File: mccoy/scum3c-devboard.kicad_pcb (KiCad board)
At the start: 2 copper layers, 42.5 x 34.3 mm, 44 parts, among them J1 Conn_02x06_Odd_Even, J10 through_hole, J11 through_hole, J12 through_hole, J13 through_hole, J14 through_hole, J15 through_hole, J16 through_hole, J17 through_hole, J18 through_hole, J19 through_hole, J2 Conn_02x10_Odd_Even, J20 through_hole, J21 through_hole, J3 Conn_02x06_Odd_Even, J4 Conn_01x01_Male, J5 through_hole, J6 through_hole, J7 through_hole, J8 through_hole, J9 through_hole, U1 scum3, U9AB1 ICM-20948

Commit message: added some labels for clarity
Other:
- board text added: "P0.15"

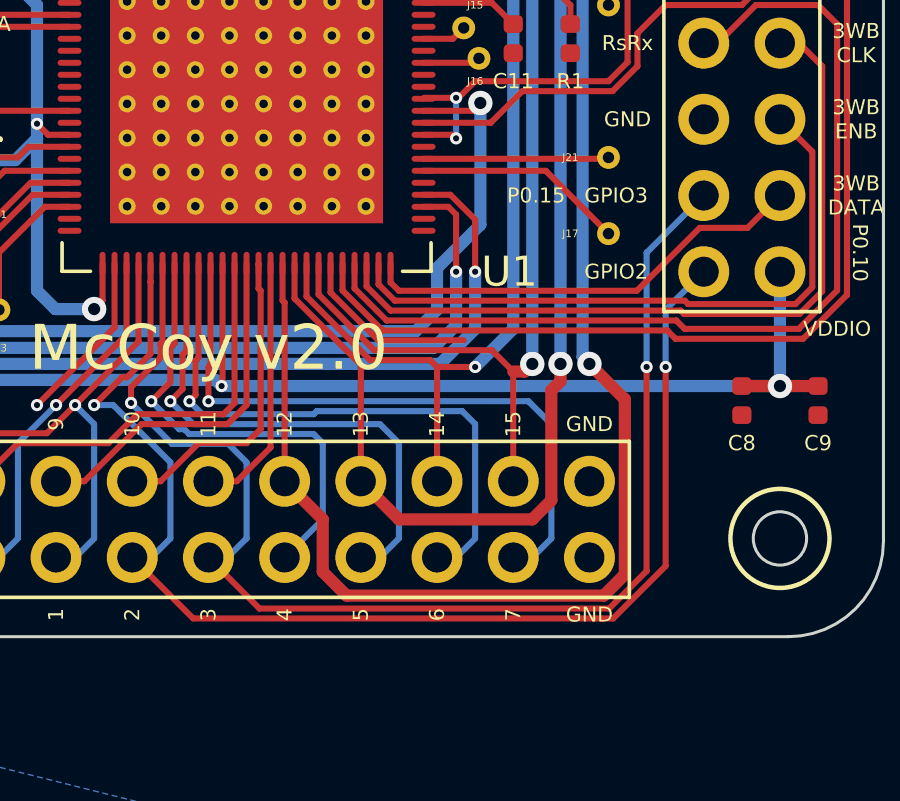
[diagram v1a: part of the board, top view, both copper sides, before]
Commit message: swapped around GPIO 2 and 3 for nrf
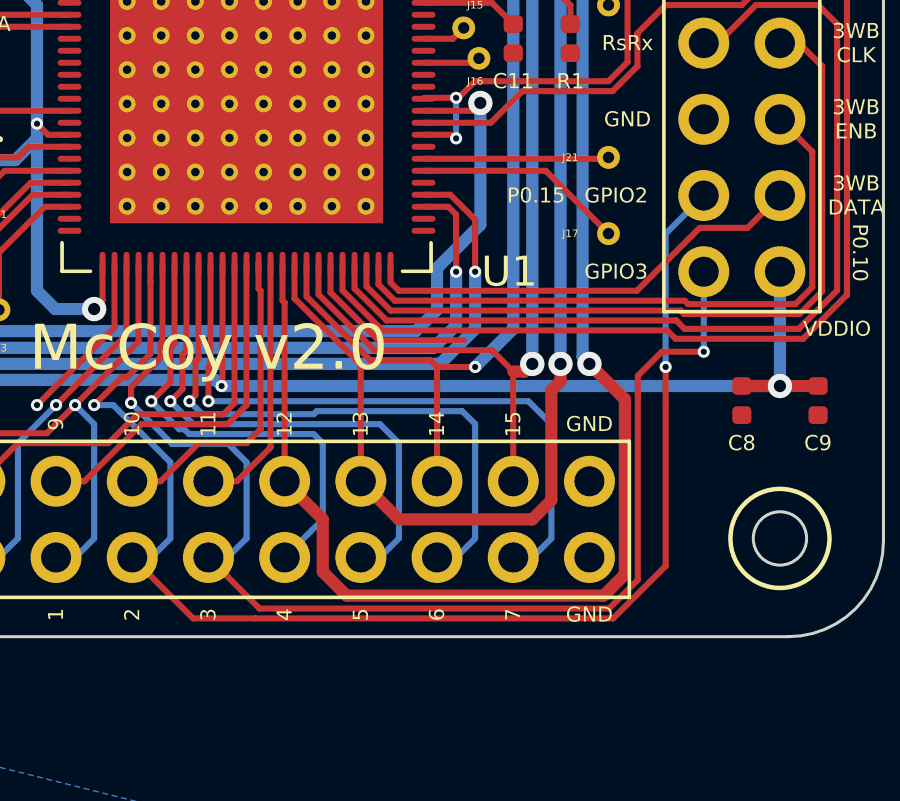
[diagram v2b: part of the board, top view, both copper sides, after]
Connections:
- J3 pad 11: /GPIO2 -> /GPIO3
- J3 pad 9: /GPIO3 -> /GPIO2
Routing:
- net /GPIO2: track 42.7 -> 45.2 mm
- net /GPIO3: track 42.9 -> 41.3 mm
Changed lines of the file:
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@@
     (thickness 1.6)
     (drawings 772)
-    (tracks 454)
+    (tracks 459)
     (zones 0)
     (modules 44)
@@
   (page A4)
   (layers
-    (0 F.Cu mixed hide)
-    (31 B.Cu mixed hide)
-    (32 B.Adhes user hide)
-    (33 F.Adhes user hide)
+    (0 F.Cu mixed)
+    (31 B.Cu mixed)
+    (32 B.Adhes user)
+    (33 F.Adhes user)
     (34 B.Paste user hide)
-    (35 F.Paste user hide)
+    (35 F.Paste user)
     (36 B.SilkS user)
     (37 F.SilkS user)
     (38 B.Mask user)
     (39 F.Mask user hide)
-    (40 Dwgs.User user hide)
-    (41 Cmts.User user hide)
-    (42 Eco1.User user hide)
-    (43 Eco2.User user hide)
+    (40 Dwgs.User user)
+    (41 Cmts.User user)
+    (42 Eco1.User user)
+    (43 Eco2.User user)
     (44 Edge.Cuts user)
-    (45 Margin user hide)
-    (46 B.CrtYd user hide)
+    (45 Margin user)
+    (46 B.CrtYd user)
     (47 F.CrtYd user)
-    (48 B.Fab user hide)
-    (49 F.Fab user hide)
+    (48 B.Fab user)
+    (49 F.Fab user)
   )
   (setup
@@
       (net 4 +VDDIO))
     (pad 11 thru_hole oval (at 0 12.7) (size 1.7 1.7) (drill 1) (layers *.Cu *.Mask)
-      (net 13 /GPIO2))
+      (net 9 /GPIO3))
     (pad 10 thru_hole oval (at 2.54 10.16) (size 1.7 1.7) (drill 1) (layers *.Cu *.Mask)
       (net 15 /3WB_DATA))
     (pad 9 thru_hole oval (at 0 10.16) (size 1.7 1.7) (drill 1) (layers *.Cu *.Mask)
-      (net 9 /GPIO3))
+      (net 13 /GPIO2))
     (pad 8 thru_hole oval (at 2.54 7.62) (size 1.7 1.7) (drill 1) (layers *.Cu *.Mask)
       (net 16 /3WB_ENB))
@@
     (effects (font (size 0.5 0.5) (thickness 0.1)) (justify mirror))
   )
-  (gr_text GPIO2 (at 138.684 96.52) (layer F.SilkS)
-    (effects (font (size 0.5 0.5) (thickness 0.1)))
-  )
-  (gr_text GPIO2 (at 138.684 96.52) (layer B.SilkS)
-    (effects (font (size 0.5 0.5) (thickness 0.1)) (justify mirror))
-  )
-  (gr_text GPIO3 (at 138.684 93.98) (layer F.SilkS)
-    (effects (font (size 0.5 0.5) (thickness 0.1)))
-  )
-  (gr_text GPIO3 (at 138.684 93.98) (layer B.SilkS)
+  (gr_text GPIO2 (at 138.684 93.98) (layer F.SilkS)
+    (effects (font (size 0.5 0.5) (thickness 0.1)))
+  )
+  (gr_text GPIO2 (at 138.684 93.98) (layer B.SilkS)
+    (effects (font (size 0.5 0.5) (thickness 0.1)) (justify mirror))
+  )
+  (gr_text GPIO3 (at 138.684 96.52) (layer F.SilkS)
+    (effects (font (size 0.5 0.5) (thickness 0.1)))
+  )
+  (gr_text GPIO3 (at 138.684 96.52) (layer B.SilkS)
     (effects (font (size 0.5 0.5) (thickness 0.1)) (justify mirror))
   )
@@
   (segment (start 125.73 106.045) (end 125.095 106.045) (width 0.2032) (layer B.Cu) (net 9) (status 30))
   (segment (start 126.365 105.41) (end 125.73 106.045) (width 0.2032) (layer B.Cu) (net 9) (status 20))
-  (via (at 139.7 99.695) (size 0.4064) (drill 0.2032) (layers F.Cu B.Cu) (net 9))
-  (segment (start 138.450559 107.74681) (end 139.7 106.497369) (width 0.2032) (layer F.Cu) (net 9))
-  (segment (start 139.7 106.497369) (end 139.7 99.695) (width 0.2032) (layer F.Cu) (net 9))
+  (segment (start 138.450559 107.74681) (end 139.407011 106.790358) (width 0.2032) (layer F.Cu) (net 9))
   (segment (start 125.095 106.045) (end 126.79681 107.74681) (width 0.2032) (layer F.Cu) (net 9))
   (segment (start 126.79681 107.74681) (end 138.450559 107.74681) (width 0.2032) (layer F.Cu) (net 9))
-  (segment (start 139.7 95.885) (end 141.605 93.98) (width 0.2032) (layer B.Cu) (net 9))
-  (segment (start 139.7 99.695) (end 139.7 95.885) (width 0.2032) (layer B.Cu) (net 9))
+  (via (at 141.605 99.18701) (size 0.4064) (drill 0.2032) (layers F.Cu B.Cu) (net 9))
+  (segment (start 141.605 99.18701) (end 141.605 96.52) (width 0.2032) (layer B.Cu) (net 9))
+  (segment (start 141.605 99.18701) (end 140.20799 99.18701) (width 0.2032) (layer F.Cu) (net 9))
+  (segment (start 140.20799 99.18701) (end 139.407011 99.987989) (width 0.2032) (layer F.Cu) (net 9))
+  (segment (start 139.407011 99.987989) (end 139.407011 100.622989) (width 0.2032) (layer F.Cu) (net 9))
+  (segment (start 139.407011 106.790358) (end 139.407011 100.622989) (width 0.2032) (layer F.Cu) (net 9))
+  (segment (start 139.407011 100.622989) (end 139.407011 100.59474) (width 0.2032) (layer F.Cu) (net 9))
   (via (at 120.65 100.965) (size 0.4064) (drill 0.2032) (layers F.Cu B.Cu) (net 10))
   (segment (start 122.765 96.255) (end 122.765 98.85) (width 0.2032) (layer F.Cu) (net 10) (status 10))
@@
   (segment (start 121.92 100.965) (end 121.285 100.965) (width 0.2032) (layer B.Cu) (net 13))
   (segment (start 123.19 106.045) (end 123.825 105.41) (width 0.2032) (layer B.Cu) (net 13) (status 10))
+  (segment (start 124.58702 108.07702) (end 126.660033 108.07702) (width 0.2032) (layer F.Cu) (net 13))
+  (segment (start 122.555 106.045) (end 124.58702 108.07702) (width 0.2032) (layer F.Cu) (net 13))
+  (segment (start 138.587336 108.07702) (end 140.335 106.329356) (width 0.2032) (layer F.Cu) (net 13))
+  (segment (start 126.660033 108.07702) (end 138.587336 108.07702) (width 0.2032) (layer F.Cu) (net 13))
+  (segment (start 140.335 106.329356) (end 140.335 100.965) (width 0.2032) (layer F.Cu) (net 13))
   (via (at 140.335 99.695) (size 0.4064) (drill 0.2032) (layers F.Cu B.Cu) (net 13))
-  (segment (start 138.587336 108.07702) (end 140.335 106.329356) (width 0.2032) (layer F.Cu) (net 13))
-  (segment (start 122.555 106.045) (end 124.58702 108.07702) (width 0.2032) (layer F.Cu) (net 13))
-  (segment (start 140.335 106.329356) (end 140.335 99.695) (width 0.2032) (layer F.Cu) (net 13))
-  (segment (start 124.58702 108.07702) (end 138.587336 108.07702) (width 0.2032) (layer F.Cu) (net 13))
-  (segment (start 140.335 97.79) (end 141.605 96.52) (width 0.2032) (layer B.Cu) (net 13))
-  (segment (start 140.335 99.695) (end 140.335 97.79) (width 0.2032) (layer B.Cu) (net 13))
+  (segment (start 140.335 100.965) (end 140.335 99.695) (width 0.2032) (layer F.Cu) (net 13))
+  (segment (start 140.335 95.25) (end 141.605 93.98) (width 0.2032) (layer B.Cu) (net 13))
+  (segment (start 140.335 99.695) (end 140.335 95.25) (width 0.2032) (layer B.Cu) (net 13))
   (via (at 120.015 100.965) (size 0.4064) (drill 0.2032) (layers F.Cu B.Cu) (net 14))
   (segment (start 122.365 96.255) (end 122.365 98.615) (width 0.2032) (layer F.Cu) (net 14) (status 10))

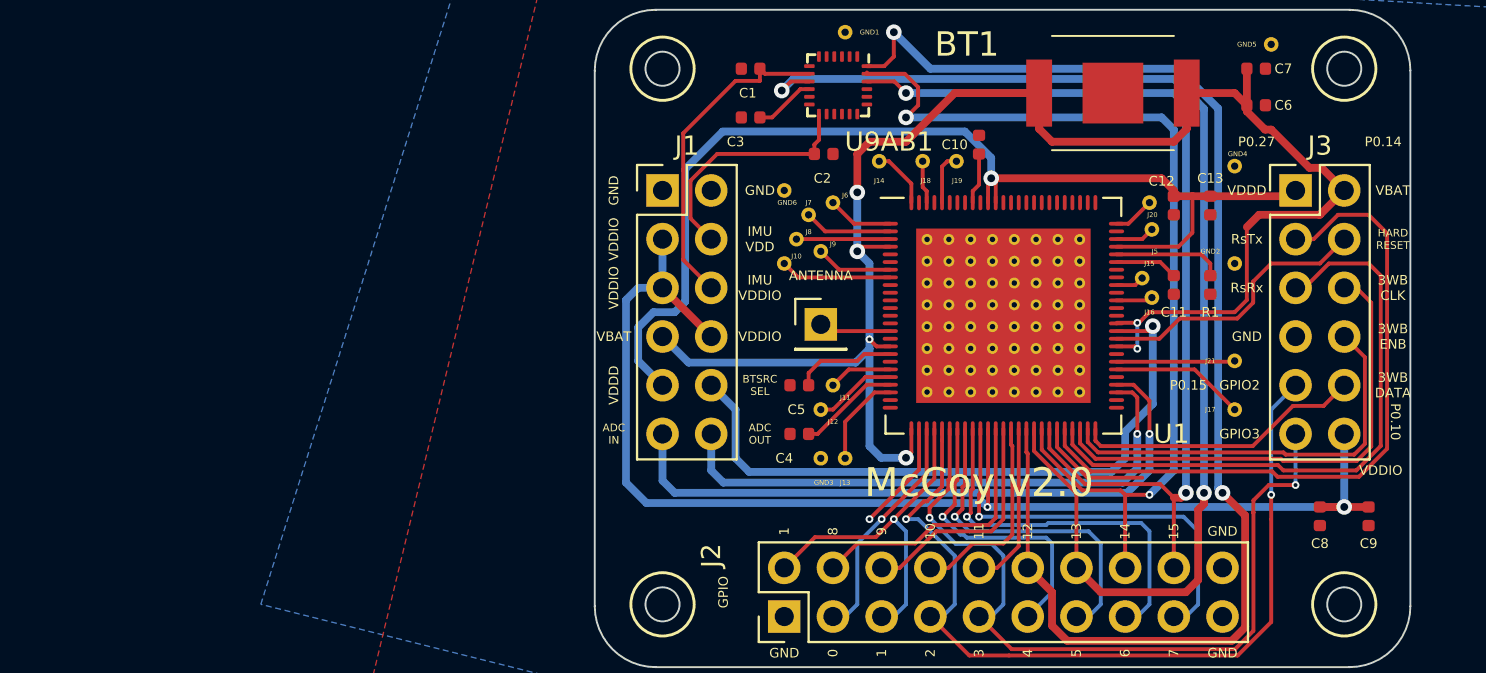
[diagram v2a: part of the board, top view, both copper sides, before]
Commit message: added a regulator to layout
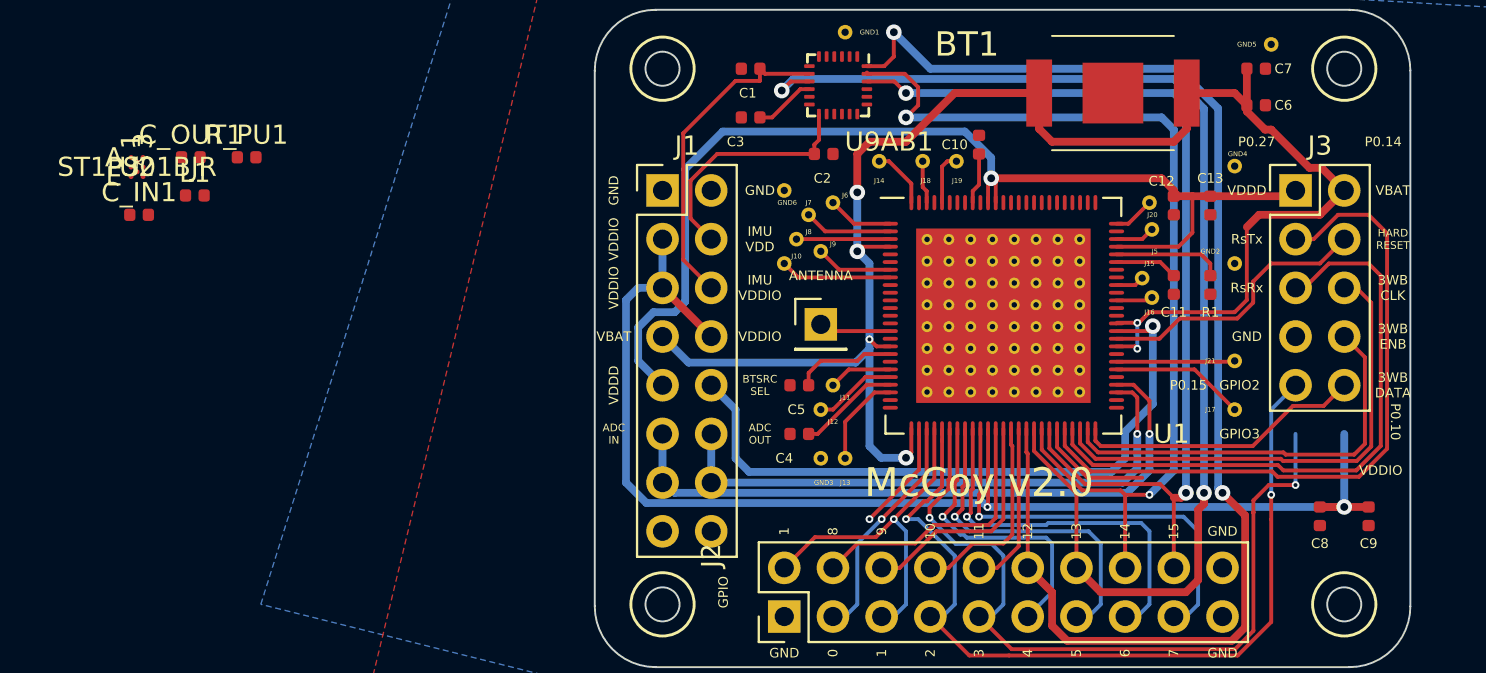
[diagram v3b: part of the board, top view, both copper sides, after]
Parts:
- added C_IN1: 10 uF, Capacitor_SMD:C_0402_1005Metric, F.Cu at (81.3, 85.1)
- added C_OUT1: 10 uF, Capacitor_SMD:C_0402_1005Metric, F.Cu at (84.0, 82.1)
- added L1: 2.2 uH, Inductor_SMD:L_0402_1005Metric, F.Cu at (84.2, 84.1)
- added R_PU1: 1M, Resistor_SMD:R_0402_1005Metric, F.Cu at (86.9, 82.1)
- added U2: ST1PS01BJR, regulator:ST1PS01BJR, F.Cu at (81.2, 82.6)
- J1: value Conn_02x06_Odd_Even -> Conn_02x08_Odd_Even; footprint Connector_PinHeader_2.54mm:PinHeader_2x06_P2.54mm_Vertical -> Connector_PinHeader_2.54mm:PinHeader_2x08_P2.54mm_Vertical
- J3: value Conn_02x06_Odd_Even -> Conn_02x05_Odd_Even; footprint Connector_PinHeader_2.54mm:PinHeader_2x06_P2.54mm_Vertical -> Connector_PinHeader_2.54mm:PinHeader_2x05_P2.54mm_Vertical
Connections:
- U1 pad 10: (no net) -> +VDD25
- U1 pad 12: (no net) -> Net-(U1-Pad12)
- U1 pad 13: (no net) -> Net-(U1-Pad13)
- U1 pad 19: (no net) -> Net-(U1-Pad19)
- U1 pad 24: (no net) -> Net-(U1-Pad24)
- U1 pad 25: (no net) -> Net-(U1-Pad25)
- U1 pad 51: (no net) -> Net-(U1-Pad51)
- U1 pad 52: (no net) -> Net-(U1-Pad52)
- U1 pad 6: (no net) -> Net-(U1-Pad6)
- U1 pad 63: (no net) -> Net-(U1-Pad63)
- U1 pad 64: (no net) -> Net-(U1-Pad64)
- U1 pad 66: (no net) -> Net-(U1-Pad66)
- U1 pad 68: (no net) -> Net-(U1-Pad68)
- U1 pad 74: (no net) -> Net-(U1-Pad74)
- U1 pad 76: (no net) -> Net-(U1-Pad76)
- U1 pad 77: (no net) -> Net-(U1-Pad77)
- U1 pad 78: (no net) -> Net-(U1-Pad78)
- U1 pad 79: (no net) -> Net-(U1-Pad79)
- U1 pad 80: (no net) -> Net-(U1-Pad80)
- U1 pad 81: (no net) -> Net-(U1-Pad81)
- U1 pad 82: (no net) -> Net-(U1-Pad82)
- U1 pad 83: (no net) -> Net-(U1-Pad83)
- U1 pad 84: (no net) -> Net-(U1-Pad84)
- U1 pad 85: (no net) -> Net-(U1-Pad85)
- U1 pad 86: (no net) -> Net-(U1-Pad86)
- U1 pad 87: (no net) -> Net-(U1-Pad87)
- U1 pad 88: (no net) -> Net-(U1-Pad88)
- U1 pad 9: (no net) -> Net-(U1-Pad9)
- U1 pad 91: (no net) -> Net-(U1-Pad91)
- U1 pad 93: (no net) -> Net-(U1-Pad93)
- U1 pad 94: (no net) -> Net-(U1-Pad94)
- U1 pad 95: (no net) -> Net-(U1-Pad95)
- U1 pad 97: (no net) -> Net-(U1-Pad97)
- U1 pad 99: (no net) -> Net-(U1-Pad99)
- U9AB1 pad 1: (no net) -> Net-(U9AB1-Pad1)
- U9AB1 pad 12: (no net) -> Net-(U9AB1-Pad12)
- U9AB1 pad 14: (no net) -> Net-(U9AB1-Pad14)
- U9AB1 pad 15: (no net) -> Net-(U9AB1-Pad15)
- U9AB1 pad 16: (no net) -> Net-(U9AB1-Pad16)
- U9AB1 pad 17: (no net) -> Net-(U9AB1-Pad17)
- U9AB1 pad 19: (no net) -> Net-(U9AB1-Pad19)
- U9AB1 pad 2: (no net) -> Net-(U9AB1-Pad2)
- U9AB1 pad 21: (no net) -> Net-(U9AB1-Pad21)
- U9AB1 pad 3: (no net) -> Net-(U9AB1-Pad3)
- U9AB1 pad 4: (no net) -> Net-(U9AB1-Pad4)
- U9AB1 pad 5: (no net) -> Net-(U9AB1-Pad5)
- U9AB1 pad 6: (no net) -> Net-(U9AB1-Pad6)
- U9AB1 pad 7: (no net) -> Net-(U9AB1-Pad7)

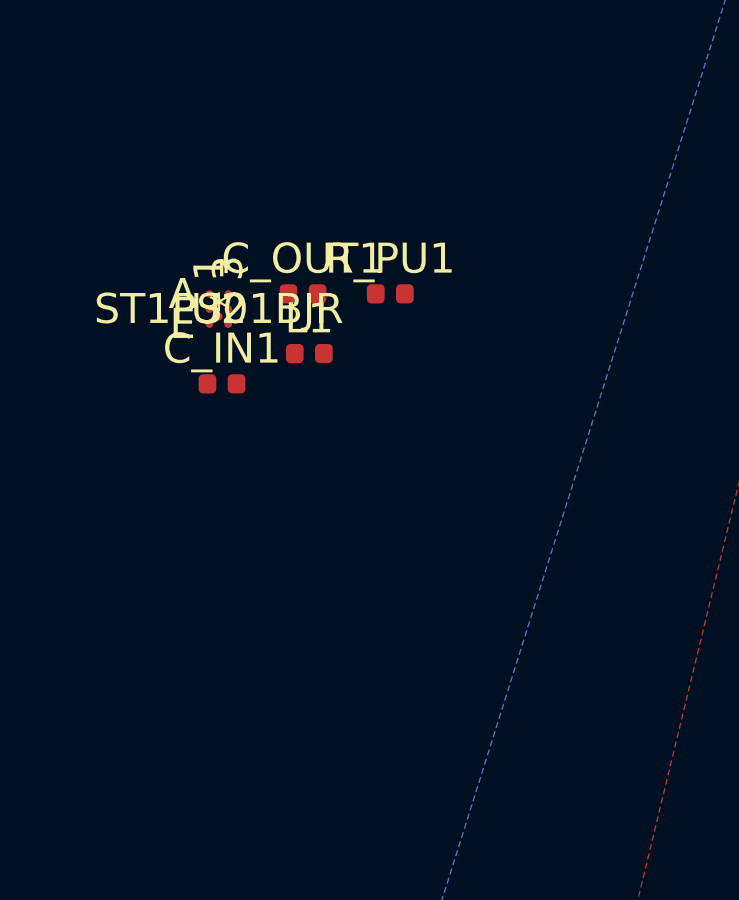
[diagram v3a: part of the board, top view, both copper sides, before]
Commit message: removed old footprints
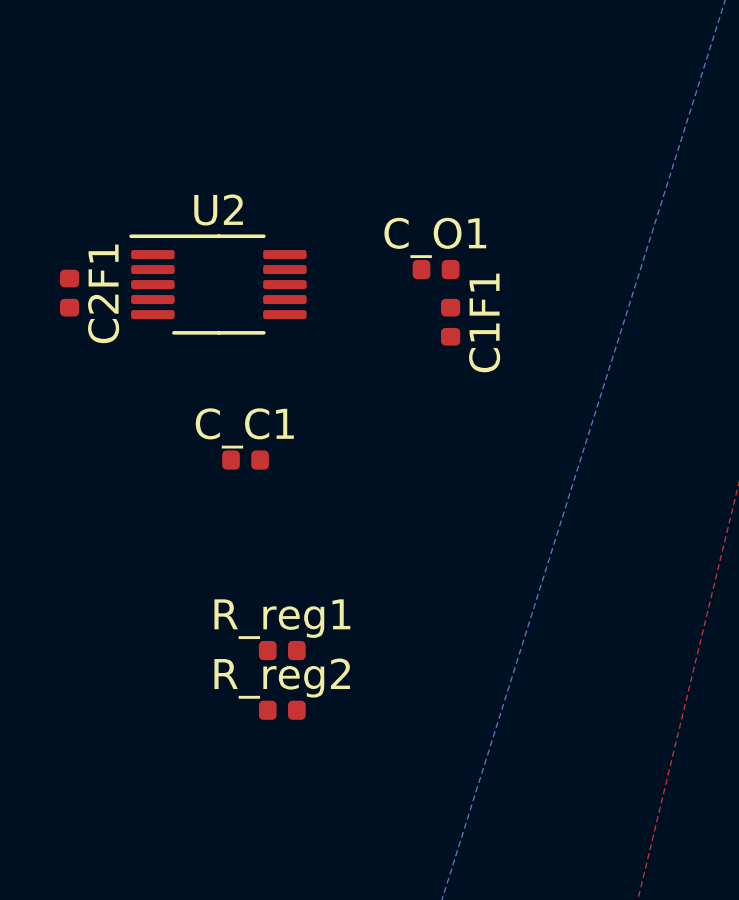
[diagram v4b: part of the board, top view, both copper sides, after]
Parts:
- removed C_IN1, C_OUT1: 10 uF, Capacitor_SMD:C_0402_1005Metric
- removed L1: 2.2 uH, Inductor_SMD:L_0402_1005Metric
- removed R_PU1: 1M, Resistor_SMD:R_0402_1005Metric
- added C1F1: 1 uF, Capacitor_SMD:C_0402_1005Metric, F.Cu at (88.9, 83.0)
- added C2F1: 1 uF, Capacitor_SMD:C_0402_1005Metric, F.Cu at (76.2, 82.1)
- added C_C1: 10 pF, Capacitor_SMD:C_0402_1005Metric, F.Cu at (82.1, 87.6)
- added C_O1: 10 uF, Capacitor_SMD:C_0402_1005Metric, F.Cu at (88.4, 81.3)
- added R_reg1: 75 k Ohm, Resistor_SMD:R_0402_1005Metric, F.Cu at (83.3, 94.0)
- added R_reg2: 200 k Ohm, Resistor_SMD:R_0402_1005Metric, F.Cu at (83.3, 96.0)
- U2: value ST1PS01BJR -> TPS60500DGS; footprint regulator:ST1PS01BJR -> Package_SO:VSSOP-10_3x3mm_P0.5mm
- moved U2 0.82 mm to (81.2, 81.8)

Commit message: moved some labels out of the way
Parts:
- moved R_reg2 10.3 mm to (81.3, 85.9), turned to 90 degrees
- moved R_reg1 8.67 mm to (86.4, 85.9), turned to 270 degrees
- moved C_C1 2.48 mm to (83.8, 85.9), turned to 270 degrees
- moved C_O1 2.02 mm to (86.8, 82.5)
- moved C1F1 1.27 mm to (90.2, 83.0)
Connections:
- C_C1 pad 2: GND -> Net-(C_C1-Pad2)
- R_reg1 pad 2: GND -> Net-(C_C1-Pad2)
- R_reg2 pad 1: GND -> Net-(C_C1-Pad2)
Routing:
- net +VBAT: track 88.7 -> 80.0 mm
